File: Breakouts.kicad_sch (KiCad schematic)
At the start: 2 parts, among them U1 ESP-07, U2 AMS1117-3_3

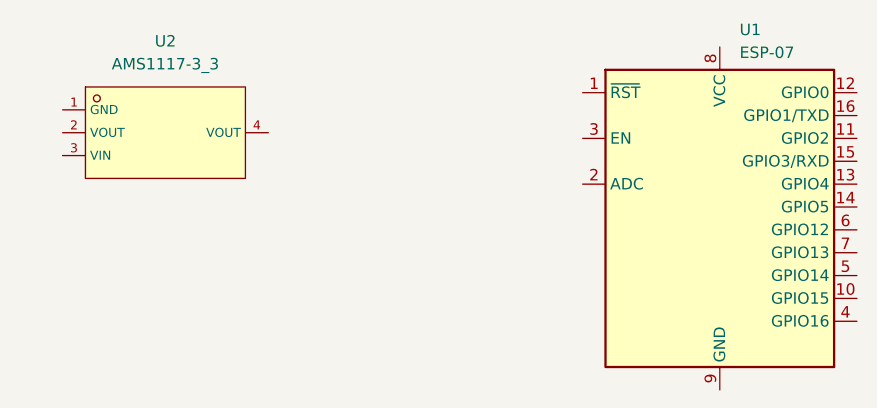
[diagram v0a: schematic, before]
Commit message: Add AMS117
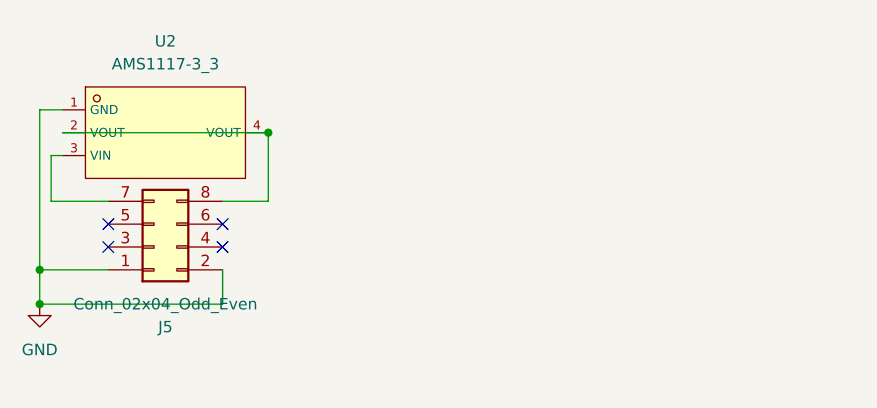
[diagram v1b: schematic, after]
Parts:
- removed U1: ESP-07, jlc_footprints:WIFIM-SMD_ESP-07, symbol RF_Module:ESP-07
- added J5: Conn_02x04_Odd_Even, Connector_PinHeader_2.54mm:PinHeader_2x04_P2.54mm_Vertical, symbol Connector_Generic:Conn_02x04_Odd_Even
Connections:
- net GND: now reaches U2.1 (GND)
- net GND: now also J5.1 (Pin_1), J5.2 (Pin_2)
- net at U2.2 (VOUT): now also U2.4 (VOUT), J5.8 (Pin_8)
- net at U2.3 (VIN): now also J5.7 (Pin_7)
- no-connect marks 0 -> 4
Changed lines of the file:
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@@
 (kicad_sch (version 20230121) (generator eeschema)
   (paper "A4")
+  (junction (at 81.28 71.12) (diameter 0) (color 0 0 0 0)
+  )
+  (junction (at 55.88 90.17) (diameter 0) (color 0 0 0 0)
+  )
+  (junction (at 55.88 86.36) (diameter 0) (color 0 0 0 0)
+  )
+  (no_connect (at 63.5 83.82))
+  (no_connect (at 76.2 81.28))
+  (no_connect (at 63.5 81.28))
+  (no_connect (at 76.2 83.82))
+  (wire (pts (xy 57.15 78.74) (xy 57.15 73.66))
+    (stroke (width 0) (type default))
+  )
+  (wire (pts (xy 63.5 78.74) (xy 57.15 78.74))
+    (stroke (width 0) (type default))
+  )
+  (wire (pts (xy 55.88 86.36) (xy 63.5 86.36))
+    (stroke (width 0) (type default))
+  )
+  (wire (pts (xy 55.88 90.17) (xy 76.2 90.17))
+    (stroke (width 0) (type default))
+  )
+  (wire (pts (xy 81.28 71.12) (xy 81.28 78.74))
+    (stroke (width 0) (type default))
+  )
+  (wire (pts (xy 58.42 68.58) (xy 55.88 68.58))
+    (stroke (width 0) (type default))
+  )
+  (wire (pts (xy 57.15 73.66) (xy 58.42 73.66))
+    (stroke (width 0) (type default))
+  )
+  (wire (pts (xy 55.88 68.58) (xy 55.88 86.36))
+    (stroke (width 0) (type default))
+  )
+  (wire (pts (xy 81.28 78.74) (xy 76.2 78.74))
+    (stroke (width 0) (type default))
+  )
+  (wire (pts (xy 58.42 71.12) (xy 81.28 71.12))
+    (stroke (width 0) (type default))
+  )
+  (wire (pts (xy 55.88 86.36) (xy 55.88 90.17))
+    (stroke (width 0) (type default))
+  )
+  (wire (pts (xy 76.2 90.17) (xy 76.2 86.36))
+    (stroke (width 0) (type default))
+  )
+  (symbol (lib_id "Connector_Generic:Conn_02x04_Odd_Even") (at 68.58 83.82 0) (mirror x) (unit 1)
+    (in_bom yes) (on_board yes) (dnp no)
+    (property "Reference" "J5" (at 69.85 92.71 0)
+      (effects (font (size 1.27 1.27)))
+    )
+    (property "Value" "Conn_02x04_Odd_Even" (at 69.85 90.17 0)
+      (effects (font (size 1.27 1.27)))
+    )
+    (property "Footprint" "Connector_PinHeader_2.54mm:PinHeader_2x04_P2.54mm_Vertical" (at 68.58 83.82 0)
+      (effects (font (size 1.27 1.27)) hide)
+    )
+    (property "Datasheet" "~" (at 68.58 83.82 0)
+      (effects (font (size 1.27 1.27)) hide)
+    )
+    (pin "7")
+    (pin "2")
+    (pin "8")
+    (pin "6")
+    (pin "5")
+    (pin "4")
+    (pin "1")
+    (pin "3")
+    (instances
+      (project "Breakouts"
+        (path "/7ebf650a-1c0b-4d71-8ef1-c883cde2ac89"
+          (reference "J5") (unit 1)
+        )
+      )
+    )
+  )
   (symbol (lib_id "jlc_symbols:AMS1117-3_3") (at 69.85 71.12 0) (unit 1)
     (in_bom yes) (on_board yes) (dnp no) (fields_autoplaced)
@@
     )
   )
-  (symbol (lib_id "RF_Module:ESP-07") (at 131.445 81.915 0) (unit 1)
+  (symbol (lib_id "power:GND") (at 55.88 90.17 0) (unit 1)
     (in_bom yes) (on_board yes) (dnp no) (fields_autoplaced)
-    (property "Reference" "U1" (at 133.6391 59.69 0)
-      (effects (font (size 1.27 1.27)) (justify left))
-    )
-    (property "Value" "ESP-07" (at 133.6391 62.23 0)
-      (effects (font (size 1.27 1.27)) (justify left))
-    )
-    (property "Footprint" "jlc_footprints:WIFIM-SMD_ESP-07" (at 131.445 81.915 0)
+    (property "Reference" "#PWR01" (at 55.88 96.52 0)
       (effects (font (size 1.27 1.27)) hide)
     )
-    (property "Datasheet" "http://wiki.ai-thinker.com/_media/esp8266/esp8266_series_modules_user_manual_v1.1.pdf" (at 122.555 79.375 0)
+    (property "Value" "GND" (at 55.88 95.25 0)
+      (effects (font (size 1.27 1.27)))
+    )
+    (property "Footprint" "" (at 55.88 90.17 0)
       (effects (font (size 1.27 1.27)) hide)
     )
-    (pin "3")
-    (pin "2")
-    (pin "7")
-    (pin "6")
-    (pin "9")
-    (pin "16")
-    (pin "15")
-    (pin "8")
-    (pin "5")
-    (pin "14")
-    (pin "11")
-    (pin "12")
-    (pin "13")
+    (property "Datasheet" "" (at 55.88 90.17 0)
+      (effects (font (size 1.27 1.27)) hide)
+    )
     (pin "1")
-    (pin "4")
-    (pin "10")
     (instances
       (project "Breakouts"
         (path "/7ebf650a-1c0b-4d71-8ef1-c883cde2ac89"
-          (reference "U1") (unit 1)
+          (reference "#PWR01") (unit 1)
         )
       )

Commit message: Add preliminary esp07
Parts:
- added J1, J2, J3, J4: Conn_01x08, Connector_PinHeader_2.54mm:PinHeader_1x08_P2.54mm_Vertical, symbol Connector_Generic:Conn_01x08
- added U1: ESP-07, jlc_footprints:WIFIM-SMD_ESP-07, symbol jlc_symbols:ESP-07
- added U3: ESP-12E, jlc_footprints:WIFIM-SMD_ESP-07, symbol ESP8266:ESP-12E
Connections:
- new net: J1.1 (Pin_1), U3.1 (REST)
- new net: J2.2 (Pin_2), U3.10 (GPIO15)
- new net: J2.3 (Pin_3), U3.11 (GPIO2)
- new net: J2.4 (Pin_4), U3.12 (GPIO0)
- new net: J2.5 (Pin_5), U3.13 (GPIO4)
- new net: J2.6 (Pin_6), U3.14 (GPIO5)
- new net: J2.7 (Pin_7), U3.15 (RXD)
- new net: J2.8 (Pin_8), U3.16 (TXD)
- new net: J1.2 (Pin_2), U3.2 (ADC)
- new net: J1.3 (Pin_3), U3.3 (CH_PD)
- new net: J1.4 (Pin_4), U3.4 (GPIO16)
- new net: J1.5 (Pin_5), U3.5 (GPIO14)
- new net: J1.6 (Pin_6), U3.6 (GPIO12)
- new net: J1.7 (Pin_7), U3.7 (GPIO13)
- new net: J1.8 (Pin_8), U3.8 (VCC)
- new net: J2.1 (Pin_1), U3.9 (GND)
- new net: J3.1 (Pin_1), U1.1 (REST)
- new net: J4.2 (Pin_2), U1.10 (GPIO15)
- new net: J4.3 (Pin_3), U1.11 (GPIO2)
- new net: J4.4 (Pin_4), U1.12 (GPIO0)
- new net: J4.5 (Pin_5), U1.13 (GPIO4)
- new net: J4.6 (Pin_6), U1.14 (GPIO5)
- new net: J4.7 (Pin_7), U1.15 (RXD0)
- new net: J4.8 (Pin_8), U1.16 (TXD0)
- new net: J3.2 (Pin_2), U1.2 (ADC)
- new net: J3.3 (Pin_3), U1.3 (CH_PD)
- new net: J3.4 (Pin_4), U1.4 (GPIO16)
- new net: J3.5 (Pin_5), U1.5 (GPIO14)
- new net: J3.6 (Pin_6), U1.6 (GPIO12)
- new net: J3.7 (Pin_7), U1.7 (GPIO13)
- new net: J3.8 (Pin_8), U1.8 (VCC)
- new net: J4.1 (Pin_1), U1.9 (GND)
- no-connect marks 4 -> 10
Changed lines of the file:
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@@
   (junction (at 55.88 86.36) (diameter 0) (color 0 0 0 0)
   )
+  (no_connect (at 193.04 59.055))
   (no_connect (at 63.5 83.82))
   (no_connect (at 76.2 81.28))
   (no_connect (at 63.5 81.28))
+  (no_connect (at 203.2 59.055))
   (no_connect (at 76.2 83.82))
+  (no_connect (at 190.5 59.055))
+  (no_connect (at 200.66 59.055))
+  (no_connect (at 195.58 59.055))
+  (no_connect (at 198.12 59.055))
   (wire (pts (xy 57.15 78.74) (xy 57.15 73.66))
     (stroke (width 0) (type default))
@@
     )
   )
+  (symbol (lib_id "ESP8266:ESP-12E") (at 196.85 36.195 0) (unit 1)
+    (in_bom yes) (on_board yes) (dnp no) (fields_autoplaced)
+    (property "Reference" "U3" (at 196.85 16.129 0)
+      (effects (font (size 1.27 1.27)))
+    )
+    (property "Value" "ESP-12E" (at 196.85 18.669 0)
+      (effects (font (size 1.27 1.27)))
+    )
+    (property "Footprint" "jlc_footprints:WIFIM-SMD_ESP-07" (at 196.85 36.195 0)
+      (effects (font (size 1.27 1.27)) hide)
+    )
+    (property "Datasheet" "http://l0l.org.uk/2014/12/esp8266-modules-hardware-guide-gotta-catch-em-all/" (at 196.85 36.195 0)
+      (effects (font (size 1.27 1.27)) hide)
+    )
+    (pin "1")
+    (pin "10")
+    (pin "11")
+    (pin "12")
+    (pin "13")
+    (pin "14")
+    (pin "15")
+    (pin "16")
+    (pin "17")
+    (pin "18")
+    (pin "19")
+    (pin "2")
+    (pin "20")
+    (pin "21")
+    (pin "22")
+    (pin "3")
+    (pin "4")
+    (pin "5")
+    (pin "6")
+    (pin "7")
+    (pin "8")
+    (pin "9")
+    (instances
+      (project "Breakouts"
+        (path "/7ebf650a-1c0b-4d71-8ef1-c883cde2ac89"
+          (reference "U3") (unit 1)
+        )
+      )
+    )
+  )
+  (symbol (lib_id "Connector_Generic:Conn_01x08") (at 168.91 36.195 0) (mirror y) (unit 1)
+    (in_bom yes) (on_board yes) (dnp no) (fields_autoplaced)
+    (property "Reference" "J1" (at 168.91 25.019 0)
+      (effects (font (size 1.27 1.27)))
+    )
+    (property "Value" "Conn_01x08" (at 168.91 25.019 0)
+      (effects (font (size 1.27 1.27)) hide)
+    )
+    (property "Footprint" "Connector_PinHeader_2.54mm:PinHeader_1x08_P2.54mm_Vertical" (at 168.91 36.195 0)
+      (effects (font (size 1.27 1.27)) hide)
+    )
+    (property "Datasheet" "~" (at 168.91 36.195 0)
+      (effects (font (size 1.27 1.27)) hide)
+    )
+    (pin "1")
+    (pin "2")
+    (pin "3")
+    (pin "4")
+    (pin "5")
+    (pin "6")
+    (pin "7")
+    (pin "8")
+    (instances
+      (project "Breakouts"
+        (path "/7ebf650a-1c0b-4d71-8ef1-c883cde2ac89"
+          (reference "J1") (unit 1)
+        )
+      )
+    )
+  )
   (symbol (lib_id "power:GND") (at 55.88 90.17 0) (unit 1)
     (in_bom yes) (on_board yes) (dnp no) (fields_autoplaced)
@@
         )
       )
+    )
+  )
+  (symbol (lib_id "jlc_symbols:ESP-07") (at 112.395 36.195 0) (unit 1)
+    (in_bom yes) (on_board yes) (dnp no) (fields_autoplaced)
+    (property "Reference" "U1" (at 112.395 23.495 0)
+      (effects (font (size 1.27 1.27)))
+    )
+    (property "Value" "ESP-07" (at 112.395 26.035 0)
+      (effects (font (size 1.27 1.27)))
+    )
+    (property "Footprint" "jlc_footprints:WIFIM-SMD_ESP-07" (at 112.395 55.245 0)
+      (effects (font (size 1.27 1.27) italic) hide)
+    )
+    (property "Datasheet" "https://so.szlcsc.com/global.html?k=C82894&ref=editor" (at 110.109 44.958 0)
+      (effects (font (size 1.27 1.27)) (justify left) hide)
+    )
+    (property "LCSC" "C82894" (at 112.395 45.085 0)
+      (effects (font (size 1.27 1.27)) hide)
+    )
+    (pin "11")
+    (pin "1")
+    (pin "5")
+    (pin "10")
+    (pin "3")
+    (pin "6")
+    (pin "7")
+    (pin "4")
+    (pin "8")
+    (pin "9")
+    (pin "12")
+    (pin "13")
+    (pin "14")
+    (pin "15")
+    (pin "16")
+    (pin "2")
+    (instances
+      (project "Breakouts"
+        (path "/7ebf650a-1c0b-4d71-8ef1-c883cde2ac89"
+          (reference "U1") (unit 1)
+        )
+      )
+    )
+  )
+  (symbol (lib_id "Connector_Generic:Conn_01x08") (at 84.455 36.195 0) (mirror y) (unit 1)
+    (in_bom yes) (on_board yes) (dnp no) (fields_autoplaced)
+    (property "Reference" "J3" (at 84.455 25.019 0)
+      (effects (font (size 1.27 1.27)))
+    )
+    (property "Value" "Conn_01x08" (at 84.455 25.019 0)
+      (effects (font (size 1.27 1.27)) hide)
+    )
+    (property "Footprint" "Connector_PinHeader_2.54mm:PinHeader_1x08_P2.54mm_Vertical" (at 84.455 36.195 0)
+      (effects (font (size 1.27 1.27)) hide)
+    )
+    (property "Datasheet" "~" (at 84.455 36.195 0)
+      (effects (font (size 1.27 1.27)) hide)
+    )
+    (pin "1")
+    (pin "2")
+    (pin "3")
+    (pin "4")
+    (pin "5")
+    (pin "6")
+    (pin "7")
+    (pin "8")
+    (instances
+      (project "Breakouts"
+        (path "/7ebf650a-1c0b-4d71-8ef1-c883cde2ac89"
+          (reference "J3") (unit 1)
+        )
+      )
+    )
+  )
+  (symbol (lib_id "Connector_Generic:Conn_01x08") (at 140.335 38.735 0) (mirror x) (unit 1)
+    (in_bom yes) (on_board yes) (dnp no) (fields_autoplaced)
+    (property "Reference" "J4" (at 140.335 24.257 0)
+      (effects (font (size 1.27 1.27)))
+    )
+    (property "Value" "Conn_01x08" (at 140.335 49.911 0)
+      (effects (font (size 1.27 1.27)) hide)
+    )
+    (property "Footprint" "Connector_PinHeader_2.54mm:PinHeader_1x08_P2.54mm_Vertical" (at 140.335 38.735 0)
+      (effects (font (size 1.27 1.27)) hide)
+    )
+    (property "Datasheet" "~" (at 140.335 38.735 0)
+      (effects (font (size 1.27 1.27)) hide)
+    )
+    (pin "1")
+    (pin "2")
+    (pin "3")
+    (pin "4")
+    (pin "5")
+    (pin "6")
+    (pin "7")
+    (pin "8")
+    (instances
+      (project "Breakouts"
+        (path "/7ebf650a-1c0b-4d71-8ef1-c883cde2ac89"
+          (reference "J4") (unit 1)
+        )
+      )
+    )
+  )
+  (symbol (lib_id "Connector_Generic:Conn_01x08") (at 224.79 38.735 0) (mirror x) (unit 1)
+    (in_bom yes) (on_board yes) (dnp no) (fields_autoplaced)
+    (property "Reference" "J2" (at 224.79 24.257 0)
+      (effects (font (size 1.27 1.27)))
+    )
+    (property "Value" "Conn_01x08" (at 224.79 49.911 0)
+      (effects (font (size 1.27 1.27)) hide)
+    )
+    (property "Footprint" "Connector_PinHeader_2.54mm:PinHeader_1x08_P2.54mm_Vertical" (at 224.79 38.735 0)
+      (effects (font (size 1.27 1.27)) hide)
+    )
+    (property "Datasheet" "~" (at 224.79 38.735 0)
+      (effects (font (size 1.27 1.27)) hide)
+    )
+    (pin "1")
+    (pin "2")
+    (pin "3")
+    (pin "4")
+    (pin "5")
+    (pin "6")
+    (pin "7")
+    (pin "8")
+    (instances
+      (project "Breakouts"
+        (path "/7ebf650a-1c0b-4d71-8ef1-c883cde2ac89"
+          (reference "J2") (unit 1)
+        )
+      )

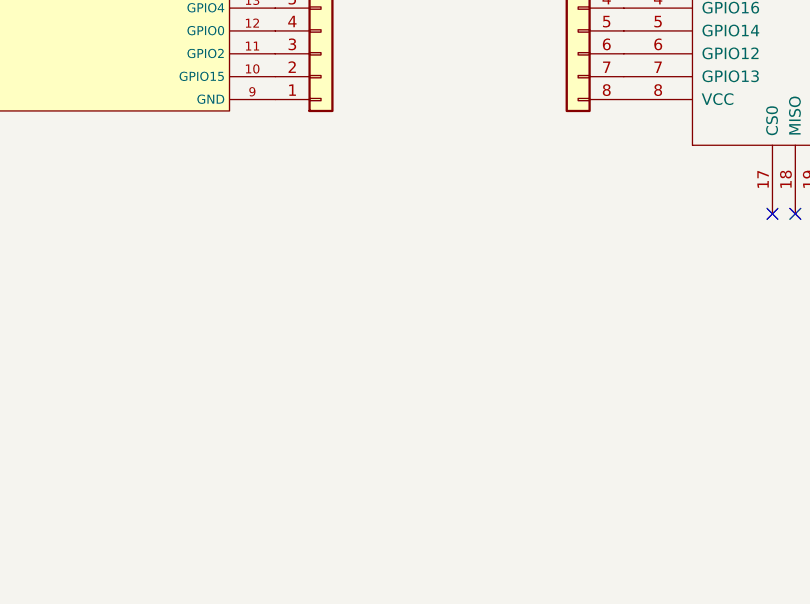
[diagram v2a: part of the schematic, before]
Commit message: Added relay breakout
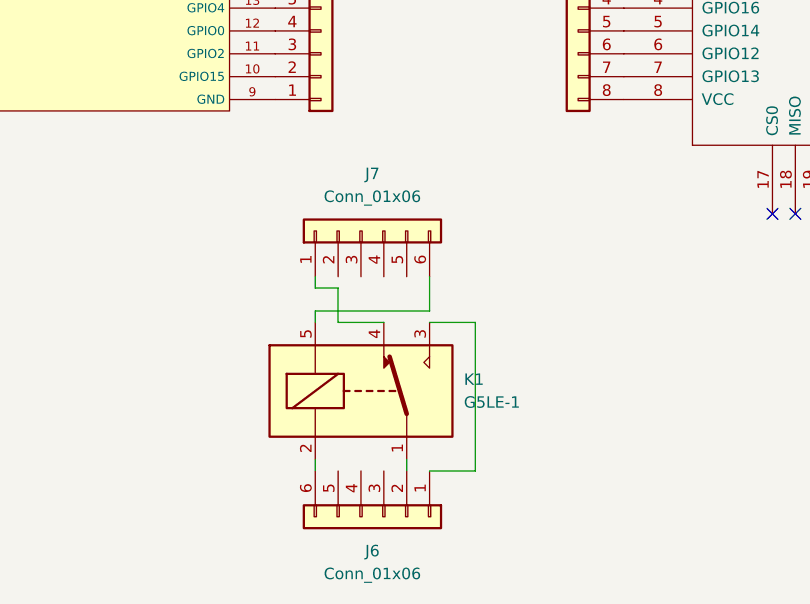
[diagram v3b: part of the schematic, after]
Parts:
- added J6, J7: Conn_01x06, Connector_PinHeader_2.54mm:PinHeader_1x06_P2.54mm_Vertical, symbol Connector_Generic:Conn_01x06
- added K1: G5LE-1, Relay_THT:Relay_SPDT_Omron-G5LE-1, symbol Relay:G5LE-1
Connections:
- new net: J6.1 (Pin_1), K1.3
- new net: J6.2 (Pin_2), K1.1
- new net: J6.6 (Pin_6), K1.2
- new net: J7.1 (Pin_1), K1.4
- new net: J7.6 (Pin_6), K1.5
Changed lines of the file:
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@@
   (no_connect (at 195.58 59.055))
   (no_connect (at 198.12 59.055))
+  (wire (pts (xy 139.7 67.31) (xy 139.7 66.04))
+    (stroke (width 0) (type default))
+  )
+  (wire (pts (xy 139.7 69.85) (xy 139.7 71.12))
+    (stroke (width 0) (type default))
+  )
+  (wire (pts (xy 142.24 67.31) (xy 139.7 67.31))
+    (stroke (width 0) (type default))
+  )
   (wire (pts (xy 57.15 78.74) (xy 57.15 73.66))
     (stroke (width 0) (type default))
@@
     (stroke (width 0) (type default))
   )
+  (wire (pts (xy 152.4 69.85) (xy 139.7 69.85))
+    (stroke (width 0) (type default))
+  )
+  (wire (pts (xy 147.32 71.12) (xy 142.24 71.12))
+    (stroke (width 0) (type default))
+  )
   (wire (pts (xy 55.88 86.36) (xy 63.5 86.36))
     (stroke (width 0) (type default))
@@
     (stroke (width 0) (type default))
   )
+  (wire (pts (xy 142.24 71.12) (xy 142.24 67.31))
+    (stroke (width 0) (type default))
+  )
+  (wire (pts (xy 152.4 71.12) (xy 157.48 71.12))
+    (stroke (width 0) (type default))
+  )
   (wire (pts (xy 81.28 71.12) (xy 81.28 78.74))
     (stroke (width 0) (type default))
@@
     (stroke (width 0) (type default))
   )
+  (wire (pts (xy 139.7 86.36) (xy 139.7 87.63))
+    (stroke (width 0) (type default))
+  )
   (wire (pts (xy 81.28 78.74) (xy 76.2 78.74))
     (stroke (width 0) (type default))
@@
     (stroke (width 0) (type default))
   )
+  (wire (pts (xy 157.48 71.12) (xy 157.48 87.63))
+    (stroke (width 0) (type default))
+  )
+  (wire (pts (xy 149.86 86.36) (xy 149.86 87.63))
+    (stroke (width 0) (type default))
+  )
+  (wire (pts (xy 152.4 66.04) (xy 152.4 69.85))
+    (stroke (width 0) (type default))
+  )
   (wire (pts (xy 55.88 86.36) (xy 55.88 90.17))
+    (stroke (width 0) (type default))
+  )
+  (wire (pts (xy 157.48 87.63) (xy 152.4 87.63))
     (stroke (width 0) (type default))
   )
@@
     )
   )
+  (symbol (lib_id "Connector_Generic:Conn_01x06") (at 147.32 92.71 270) (unit 1)
+    (in_bom yes) (on_board yes) (dnp no) (fields_autoplaced)
+    (property "Reference" "J6" (at 146.05 96.52 90)
+      (effects (font (size 1.27 1.27)))
+    )
+    (property "Value" "Conn_01x06" (at 146.05 99.06 90)
+      (effects (font (size 1.27 1.27)))
+    )
+    (property "Footprint" "Connector_PinHeader_2.54mm:PinHeader_1x06_P2.54mm_Vertical" (at 147.32 92.71 0)
+      (effects (font (size 1.27 1.27)) hide)
+    )
+    (property "Datasheet" "~" (at 147.32 92.71 0)
+      (effects (font (size 1.27 1.27)) hide)
+    )
+    (pin "6")
+    (pin "2")
+    (pin "5")
+    (pin "3")
+    (pin "4")
+    (pin "1")
+    (instances
+      (project "Breakouts"
+        (path "/7ebf650a-1c0b-4d71-8ef1-c883cde2ac89"
+          (reference "J6") (unit 1)
+        )
+      )
+    )
+  )
+  (symbol (lib_id "Relay:G5LE-1") (at 144.78 78.74 0) (unit 1)
+    (in_bom no) (on_board yes) (dnp no) (fields_autoplaced)
+    (property "Reference" "K1" (at 156.21 77.47 0)
+      (effects (font (size 1.27 1.27)) (justify left))
+    )
+    (property "Value" "G5LE-1" (at 156.21 80.01 0)
+      (effects (font (size 1.27 1.27)) (justify left))
+    )
+    (property "Footprint" "Relay_THT:Relay_SPDT_Omron-G5LE-1" (at 156.21 80.01 0)
+      (effects (font (size 1.27 1.27)) (justify left) hide)
+    )
+    (property "Datasheet" "http://www.omron.com/ecb/products/pdf/en-g5le.pdf" (at 144.78 78.74 0)
+      (effects (font (size 1.27 1.27)) hide)
+    )
+    (pin "4")
+    (pin "5")
+    (pin "2")
+    (pin "1")
+    (pin "3")
+    (instances
+      (project "Breakouts"
+        (path "/7ebf650a-1c0b-4d71-8ef1-c883cde2ac89"
+          (reference "K1") (unit 1)
+        )
+      )
+      (project "FourButtonStation"
+        (path "/fe8954b5-d30a-4533-a19e-bff77a7cd4d5"
+          (reference "K3") (unit 1)
+        )
+      )
+    )
+  )
   (symbol (lib_id "Connector_Generic:Conn_01x08") (at 168.91 36.195 0) (mirror y) (unit 1)
     (in_bom yes) (on_board yes) (dnp no) (fields_autoplaced)
@@
         )
       )
+    )
+  )
+  (symbol (lib_id "Connector_Generic:Conn_01x06") (at 144.78 60.96 90) (unit 1)
+    (in_bom yes) (on_board yes) (dnp no) (fields_autoplaced)
+    (property "Reference" "J7" (at 146.05 54.61 90)
+      (effects (font (size 1.27 1.27)))
+    )
+    (property "Value" "Conn_01x06" (at 146.05 57.15 90)
+      (effects (font (size 1.27 1.27)))
+    )
+    (property "Footprint" "Connector_PinHeader_2.54mm:PinHeader_1x06_P2.54mm_Vertical" (at 144.78 60.96 0)
+      (effects (font (size 1.27 1.27)) hide)
+    )
+    (property "Datasheet" "~" (at 144.78 60.96 0)
+      (effects (font (size 1.27 1.27)) hide)
+    )
+    (pin "6")
+    (pin "2")
+    (pin "5")
+    (pin "3")
+    (pin "4")
+    (pin "1")
+    (instances
+      (project "Breakouts"
+        (path "/7ebf650a-1c0b-4d71-8ef1-c883cde2ac89"
+          (reference "J7") (unit 1)
+        )
+      )
